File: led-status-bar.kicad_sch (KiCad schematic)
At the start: 0 parts

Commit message: Revision 1 commit
- Added all required connections to the PCB
- Fabrication revision 1
- Added README with suitable information
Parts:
- added C1, C2, C3, C4, C5: 100nF, Capacitor_SMD:C_0603_1608Metric_Pad1.08x0.95mm_HandSolder, symbol Device:C
- added D1, D2, D3, D4, D5: WS2812B, LED_SMD:LED_WS2812B_PLCC4_5.0x5.0mm_P3.2mm, symbol LED:WS2812B
- added H1, H2: MountingHole, symbol Mechanical:MountingHole
- added J1: Conn_01x03, symbol Connector_Generic:Conn_01x03
- added Q1: SS8050-G, Package_TO_SOT_SMD:SOT-23, symbol Device:Q_NPN_BCE
- added R1: 1k, Resistor_SMD:R_0603_1608Metric_Pad0.98x0.95mm_HandSolder, symbol Device:R
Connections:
- new net: D4.2 (DOUT), D5.4 (DIN)
- new net: D3.2 (DOUT), D4.4 (DIN)
- new net: D2.2 (DOUT), D3.4 (DIN)
- new net: D1.2 (DOUT), D2.4 (DIN)
- new net: Q1.1 (B), R1.1
- new net: D1.4 (DIN), Q1.3 (E)
- new net GND: C1.2, C2.2, C3.2, C4.2, C5.2, D1.3 (VSS), D2.3 (VSS), D3.3 (VSS), D4.3 (VSS), D5.3 (VSS), J1.3 (Pin_3)
- new net LED_CTRL: J1.2 (Pin_2), R1.2
- new net VSS: C1.1, C2.1, C3.1, C4.1, C5.1, D1.1 (VDD), D2.1 (VDD), D3.1 (VDD), D4.1 (VDD), D5.1 (VDD), J1.1 (Pin_1), Q1.2 (C)
- no-connect marks 0 -> 1

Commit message: Updated template for KiCAD 7
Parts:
- H1, H2: footprint (none) -> MountingHole:MountingHole_3.2mm_M3-smallBorder
- J1: footprint (none) -> Connector_PinHeader_2.54mm:PinHeader_1x03_P2.54mm_Vertical

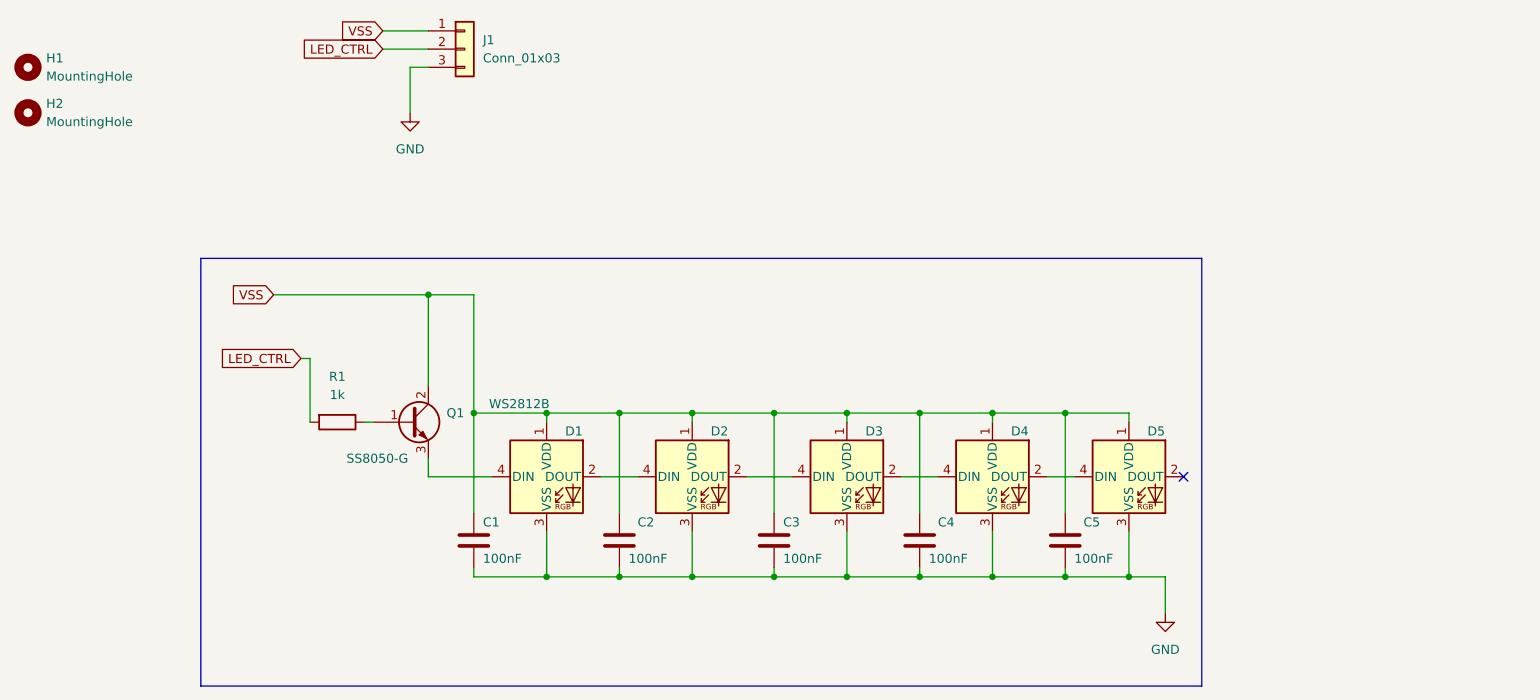
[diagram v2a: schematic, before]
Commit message: Revision 1.1 - Correcting error with Level shift
- Changed BJTs with N-Channel Mosfets
- Added resistors accordingly
- Added an outbound connector
- Added Vref (3v3) to allow daisy chaining
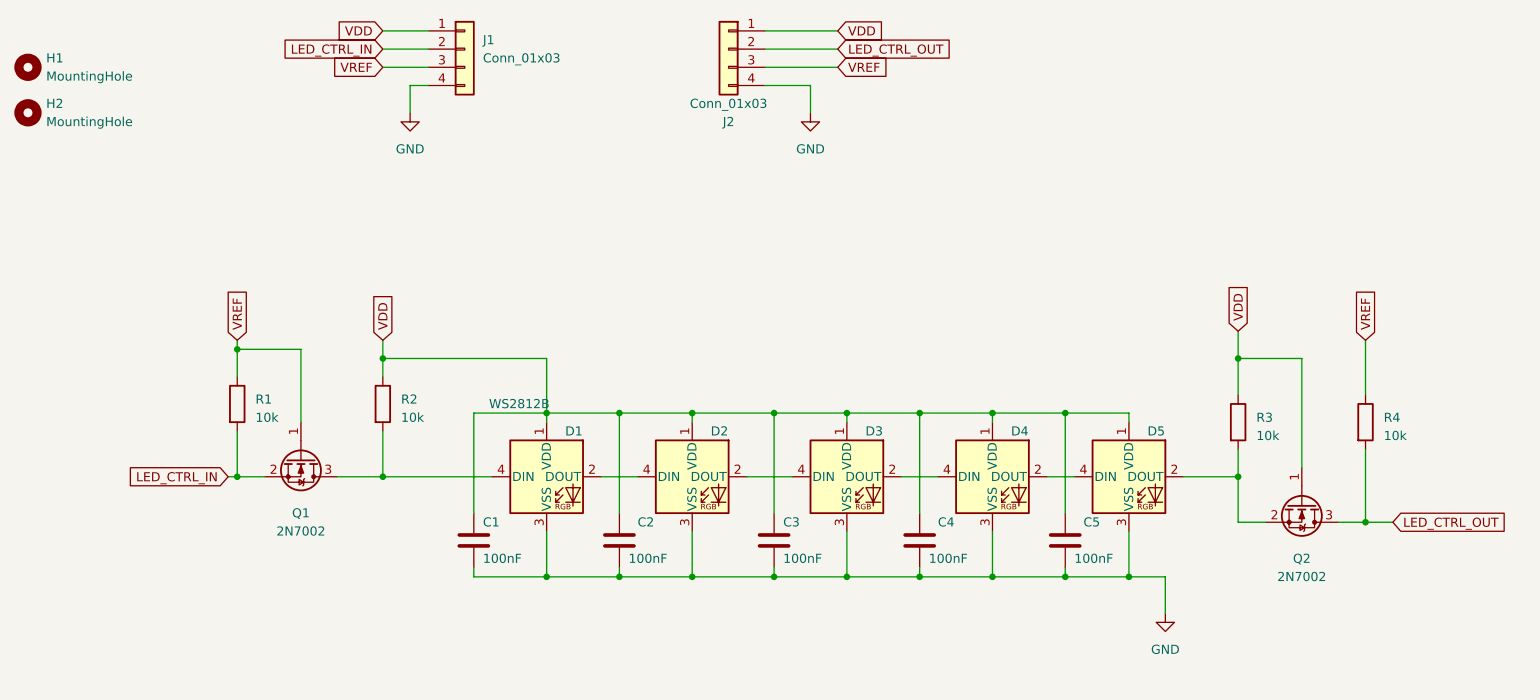
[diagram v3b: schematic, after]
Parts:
- removed Q1: SS8050-G, Package_TO_SOT_SMD:SOT-23, symbol Device:Q_NPN_BCE
- added J2: Conn_01x03, Connector_PinHeader_2.54mm:PinHeader_1x04_P2.54mm_Vertical, symbol Connector_Generic:Conn_01x04
- added Q1, Q2: 2N7002, Package_TO_SOT_SMD:SOT-23, symbol Transistor_FET:2N7002
- added R2, R3, R4: 10k, Resistor_SMD:R_0603_1608Metric_Pad0.98x0.95mm_HandSolder, symbol Device:R
- J1: footprint Connector_PinHeader_2.54mm:PinHeader_1x03_P2.54mm_Vertical -> Connector_PinHeader_2.54mm:PinHeader_1x04_P2.54mm_Vertical; symbol Connector_Generic:Conn_01x03 -> Connector_Generic:Conn_01x04
- R1: value 1k -> 10k
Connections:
- net GND: now also J1.4 (Pin_4), J2.4 (Pin_4); no longer J1.3 (Pin_3)
- net VREF: now reaches R1.1
- net VREF: now also J1.3 (Pin_3), J2.3 (Pin_3), Q1.1 (G), R4.1
- net at D5.2 (DOUT): now also Q2.2 (S), R3.2
- net at D1.4 (DIN): now also Q1.3 (D), R2.2
- net LED_CTRL renamed LED_CTRL_IN
- net LED_CTRL_IN: now also Q1.2 (S)
- net VSS renamed VDD
- net VDD: now also J2.1 (Pin_1), Q2.1 (G), R2.1, R3.1
- new net LED_CTRL_OUT: J2.2 (Pin_2), Q2.3 (D), R4.2
- no-connect marks 1 -> 0

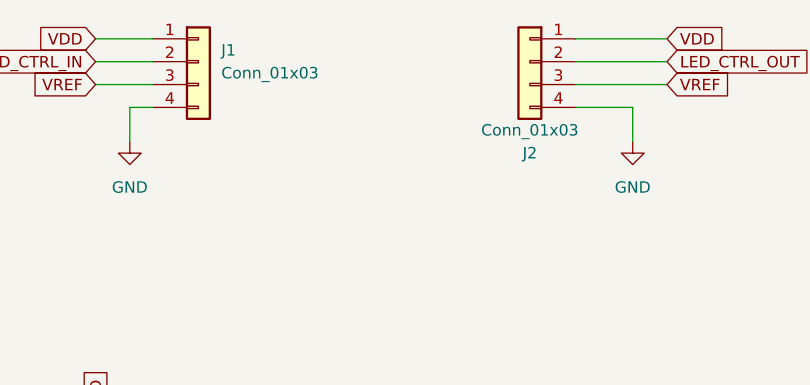
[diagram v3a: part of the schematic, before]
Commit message: Corrected fab descriptions of connectors
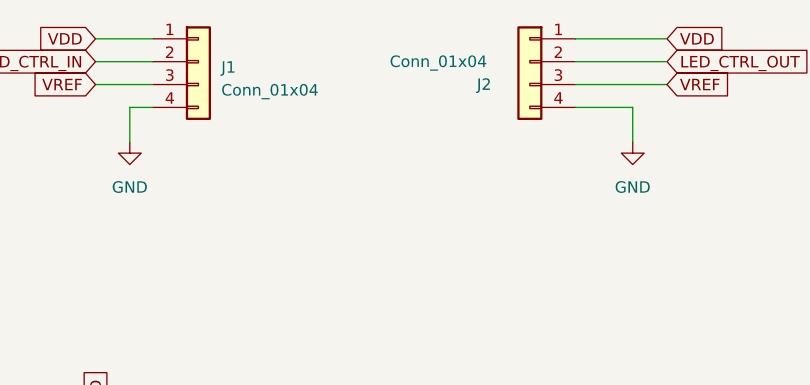
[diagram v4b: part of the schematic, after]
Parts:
- J1, J2: value Conn_01x03 -> Conn_01x04
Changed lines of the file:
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@@
   (symbol (lib_id "Connector_Generic:Conn_01x04") (at 113.03 35.56 0) (unit 1)
     (in_bom yes) (on_board yes) (dnp no) (fields_autoplaced)
-    (property "Reference" "J1" (at 115.57 34.2899 0)
+    (property "Reference" "J1" (at 115.57 36.195 0)
       (effects (font (size 1.27 1.27)) (justify left))
     )
-    (property "Value" "Conn_01x03" (at 115.57 36.8299 0)
+    (property "Value" "Conn_01x04" (at 115.57 38.735 0)
       (effects (font (size 1.27 1.27)) (justify left))
     )
@@
   (symbol (lib_id "Connector_Generic:Conn_01x04") (at 149.86 35.56 0) (mirror y) (unit 1)
     (in_bom yes) (on_board yes) (dnp no)
-    (property "Reference" "J2" (at 149.86 45.72 0)
+    (property "Reference" "J2" (at 144.78 38.1 0)
       (effects (font (size 1.27 1.27)))
     )
-    (property "Value" "Conn_01x03" (at 149.86 43.18 0)
+    (property "Value" "Conn_01x04" (at 139.7 35.56 0)
       (effects (font (size 1.27 1.27)))
     )

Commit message: Minor change: replaced pin headers with angled ones
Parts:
- J1: footprint Connector_PinHeader_2.54mm:PinHeader_1x04_P2.54mm_Vertical -> Connector_PinHeader_2.54mm:PinHeader_1x04_P2.54mm_Horizontal
- J2: footprint Connector_PinHeader_2.54mm:PinHeader_1x04_P2.54mm_Vertical -> Connector_PinSocket_2.54mm:PinSocket_1x04_P2.54mm_Horizontal
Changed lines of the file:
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@@
       (effects (font (size 1.27 1.27)) (justify left))
     )
-    (property "Footprint" "Connector_PinHeader_2.54mm:PinHeader_1x04_P2.54mm_Vertical" (at 113.03 35.56 0)
+    (property "Footprint" "Connector_PinHeader_2.54mm:PinHeader_1x04_P2.54mm_Horizontal" (at 113.03 35.56 0)
       (effects (font (size 1.27 1.27)) hide)
     )
@@
       (effects (font (size 1.27 1.27)))
     )
-    (property "Footprint" "Connector_PinHeader_2.54mm:PinHeader_1x04_P2.54mm_Vertical" (at 149.86 35.56 0)
+    (property "Footprint" "Connector_PinSocket_2.54mm:PinSocket_1x04_P2.54mm_Horizontal" (at 149.86 35.56 0)
       (effects (font (size 1.27 1.27)) hide)
     )
